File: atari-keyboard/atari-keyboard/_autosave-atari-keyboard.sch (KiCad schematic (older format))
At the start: 150 parts, among them J101 Removed LEDS. Wire soldered t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, J102 DB9_Male JOYSTICK PORT, SW101 MENU, SW102 TURBO, SW103 RESET, SW104 OPTION, SW105 SELECT, SW106 START, SW107 HELP, SW108 ESC, SW109 RSHIFT, SW110 1, SW111 2, SW112 3, SW113 4, SW114 5, SW115 6, SW116 7, SW117 8, SW118 UP, SW119 9, SW120 0, SW121 <, SW122 >, SW123 BS, SW124 BRK, SW125 TAB, SW126 Q, SW127 DOWN, SW128 W, SW129 E, SW130 R, SW131 T, SW132 Y, SW133 U, SW134 I, SW135 O, SW136 LEFT, SW137 P, SW138 [-], SW139 [=], SW140 RET, SW141 CTRL, SW142 A, SW143 S, SW144 D, SW145 RIGHT, SW146 F, SW147 G, SW148 H, SW149 J, SW150 K, SW151 L, SW152 [;], SW153 [+], SW154 MULT, SW155 CAPS, SW156 LSHIFT, SW157 Z, SW158 X, SW159 C, SW160 V, SW161 B, SW162 N, SW163 M, SW164 [,], SW165 [.], SW166 [/], SW167 FN, SW168 INV, SW169 SPC, U101 ProMicro

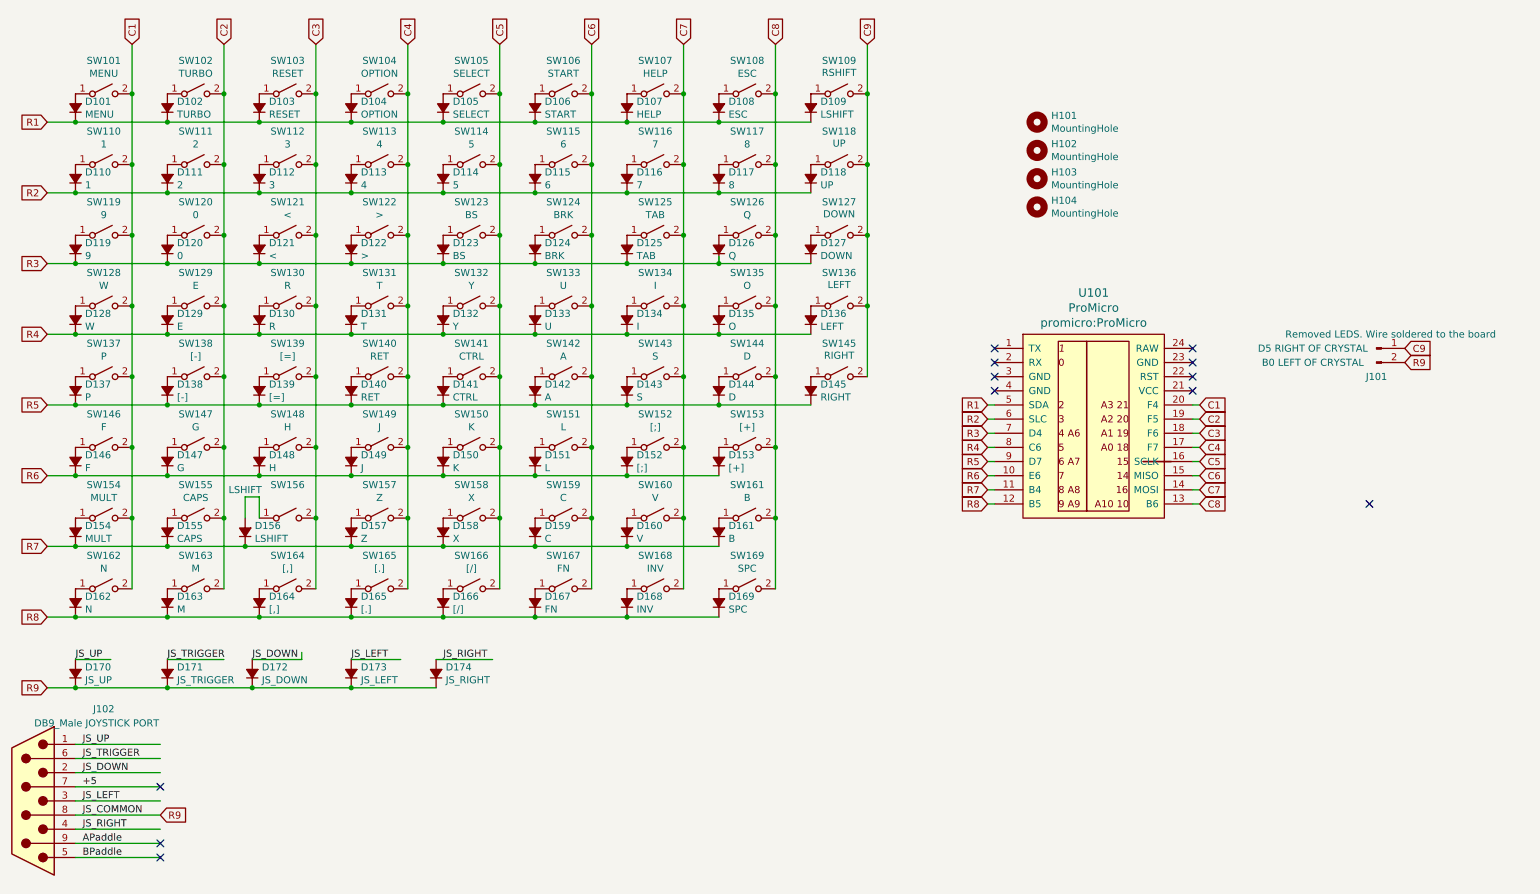
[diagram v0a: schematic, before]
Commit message: Added arrow keys and joystick support.  Writing code to auto-calc key placement.
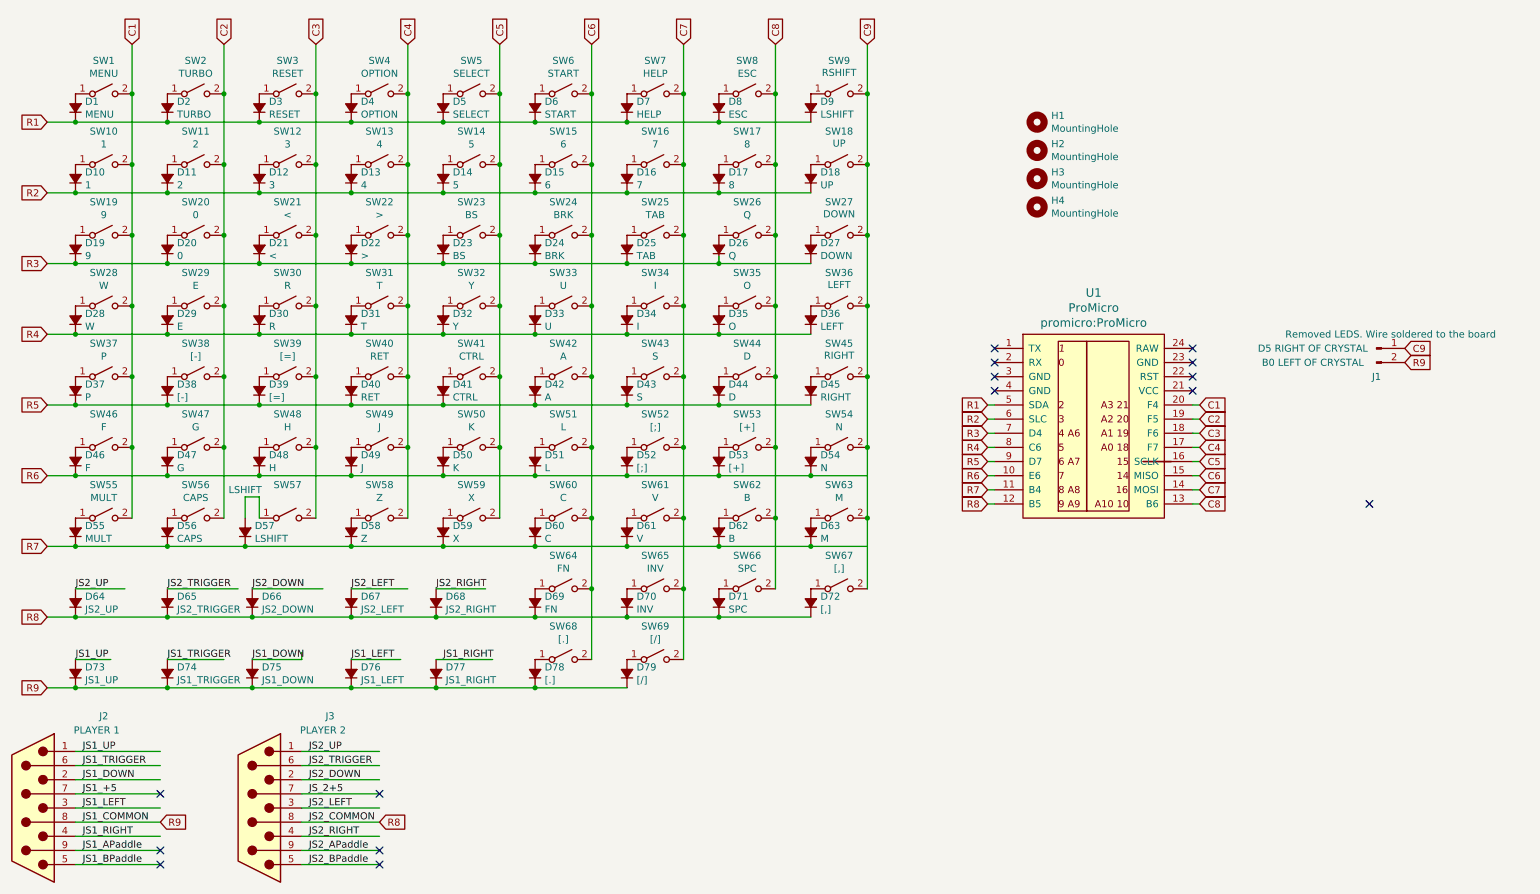
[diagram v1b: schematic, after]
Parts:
- added D65: JS2_TRIGGER, Diode_THT:D_A-405_P7.62mm_Horizontal, symbol Device:D_Small_ALT
- added D66: JS2_DOWN, Diode_THT:D_A-405_P7.62mm_Horizontal, symbol Device:D_Small_ALT
- added D67: JS2_LEFT, Diode_THT:D_A-405_P7.62mm_Horizontal, symbol Device:D_Small_ALT
- added D68: JS2_RIGHT, Diode_THT:D_A-405_P7.62mm_Horizontal, symbol Device:D_Small_ALT
- added D73: JS1_UP, Diode_THT:D_A-405_P7.62mm_Horizontal, symbol Device:D_Small_ALT
- added J3: PLAYER 2, Connector_Dsub:DSUB-9_Male_Horizontal_P2.77x2.84mm_EdgePinOffset9.90mm_Housed_MountingHolesOffset11.32mm, symbol Connector:DB9_Male
- D64: renamed from D170; value JS_UP -> JS2_UP
- D74: renamed from D171; value JS_TRIGGER -> JS1_TRIGGER
- D75: renamed from D172; value JS_DOWN -> JS1_DOWN
- D76: renamed from D173; value JS_LEFT -> JS1_LEFT
- D77: renamed from D174; value JS_RIGHT -> JS1_RIGHT
- J1: renamed from J101; footprint (none) -> Connector_PinSocket_2.54mm:PinSocket_1x02_P2.54mm_Vertical
- J2: renamed from J102; value DB9_Male JOYSTICK PORT -> PLAYER 1; footprint (none) -> Connector_Dsub:DSUB-9_Male_Horizontal_P2.77x2.84mm_EdgePinOffset9.90mm_Housed_MountingHolesOffset11.32mm
- SW18: renamed from SW118; footprint Button_Switch_Keyboard:SW_Cherry_MX_1.75u_PCB -> Button_Switch_Keyboard:SW_Cherry_MX_1.00u_PCB
- SW23: renamed from SW123; footprint Button_Switch_Keyboard:SW_Cherry_MX_1.00u_PCB -> Button_Switch_Keyboard:SW_Cherry_MX_2.00u_PCB
- SW27: renamed from SW127; footprint Button_Switch_Keyboard:SW_Cherry_MX_1.75u_PCB -> Button_Switch_Keyboard:SW_Cherry_MX_1.00u_PCB
- SW36: renamed from SW136; footprint Button_Switch_Keyboard:SW_Cherry_MX_1.75u_PCB -> Button_Switch_Keyboard:SW_Cherry_MX_1.00u_PCB
- SW45: renamed from SW145; footprint Button_Switch_Keyboard:SW_Cherry_MX_1.75u_PCB -> Button_Switch_Keyboard:SW_Cherry_MX_1.00u_PCB
- renumbered D101 to D1, D110 to D10, D111 to D11, D112 to D12, D113 to D13, D114 to D14, D115 to D15, D116 to D16, D117 to D17, D118 to D18, D119 to D19, D102 to D2, D120 to D20, D121 to D21, D122 to D22, D123 to D23, D124 to D24, D125 to D25, D126 to D26, D127 to D27, D128 to D28, D129 to D29, D103 to D3, D130 to D30, D131 to D31, D132 to D32, D133 to D33, D134 to D34, D135 to D35, D136 to D36, D137 to D37, D138 to D38, D139 to D39, D104 to D4, D140 to D40, D141 to D41, D142 to D42, D143 to D43, D144 to D44, D145 to D45, D146 to D46, D147 to D47, D148 to D48, D149 to D49, D105 to D5, D150 to D50, D151 to D51, D152 to D52, D153 to D53, D162 to D54, D154 to D55, D155 to D56, D156 to D57, D157 to D58, D158 to D59, D106 to D6, D159 to D60, D160 to D61, D161 to D62, D163 to D63, D167 to D69, D107 to D7, D168 to D70, D169 to D71, D164 to D72, D165 to D78, D166 to D79, D108 to D8, D109 to D9, H101 to H1, H102 to H2, H103 to H3, H104 to H4, SW101 to SW1, SW110 to SW10, SW111 to SW11, SW112 to SW12, SW113 to SW13, SW114 to SW14, SW115 to SW15, SW116 to SW16, SW117 to SW17, SW119 to SW19, SW102 to SW2, SW120 to SW20, SW121 to SW21, SW122 to SW22, SW124 to SW24, SW125 to SW25, SW126 to SW26, SW128 to SW28, SW129 to SW29, SW103 to SW3, SW130 to SW30, SW131 to SW31, SW132 to SW32, SW133 to SW33, SW134 to SW34, SW135 to SW35, SW137 to SW37, SW138 to SW38, SW139 to SW39, SW104 to SW4, SW140 to SW40, SW141 to SW41, SW142 to SW42, SW143 to SW43, SW144 to SW44, SW146 to SW46, SW147 to SW47, SW148 to SW48, SW149 to SW49, SW105 to SW5, SW150 to SW50, SW151 to SW51, SW152 to SW52, SW153 to SW53, SW162 to SW54, SW154 to SW55, SW155 to SW56, SW156 to SW57, SW157 to SW58, SW158 to SW59, SW106 to SW6, SW159 to SW60, SW160 to SW61, SW161 to SW62, SW163 to SW63, SW167 to SW64, SW168 to SW65, SW169 to SW66, SW164 to SW67, SW165 to SW68, SW166 to SW69, SW107 to SW7, SW108 to SW8, SW109 to SW9, U101 to U1
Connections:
- net labels added: JS1_+5, JS1_APaddle, JS1_BPaddle, JS1_COMMON, JS1_DOWN, JS1_LEFT, JS1_RIGHT, JS1_TRIGGER, JS1_UP, JS2_APaddle, JS2_BPaddle, JS2_COMMON, JS2_DOWN, JS2_LEFT, JS2_RIGHT, JS2_TRIGGER, JS2_UP, JS_2+5
- net labels removed: +5, APaddle, BPaddle, JS_COMMON, JS_DOWN, JS_LEFT, JS_RIGHT, JS_TRIGGER, JS_UP
- wire segments 178 -> 199
- no-connect marks 12 -> 15
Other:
- moved on the sheet: D54, D63, D64, D72, D78, D79, J2, SW54, SW63, SW67, SW68, SW69
